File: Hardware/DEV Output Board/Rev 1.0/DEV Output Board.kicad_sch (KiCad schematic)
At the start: 7 parts, among them J1 SPEAKER, J2 SERIAL, U1 Waveshare 2.4in LCD Header, U2 Teensy4.0, U3 Waveshare 2.4in LCD

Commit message: Add BOMs
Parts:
- U1: now in the parts list
- U2: Other (none) -> https://www.pjrc.com/store/teensy40.html
- U3: Other (none) -> https://www.amazon.com/dp/B08H24H7KX; now in the parts list
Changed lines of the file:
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@@
+			)
+		)
+		(property "Digikey" ""
+			(at 209.55 127 0)
+			(hide yes)
+			(show_name no)
+			(do_not_autoplace no)
+			(effects
+				(font
+					(size 1.27 1.27)
+				)
+			)
+		)
+		(property "Other" ""
+			(at 209.55 127 0)
+			(hide yes)
+			(show_name no)
+			(do_not_autoplace no)
+			(effects
+				(font
+					(size 1.27 1.27)
+				)
 			)
 		)
@@
 		(body_style 1)
 		(exclude_from_sim no)
-		(in_bom no)
+		(in_bom yes)
 		(on_board yes)
 		(in_pos_files yes)
@@
 		)
 		(property "Description" ""
+			(at 220.98 72.39 0)
+			(hide yes)
+			(show_name no)
+			(do_not_autoplace no)
+			(effects
+				(font
+					(size 1.27 1.27)
+				)
+			)
+		)
+		(property "Digikey" ""
+			(at 220.98 72.39 0)
+			(hide yes)
+			(show_name no)
+			(do_not_autoplace no)
+			(effects
+				(font
+					(size 1.27 1.27)
+				)
+			)
+		)
+		(property "Other" ""
 			(at 220.98 72.39 0)
 			(hide yes)
@@
 		)
 		(property "Description" "Generic connector, single row, 01x04, script generated (kicad-library-utils/schlib/autogen/connector/)"
+			(at 82.55 163.83 0)
+			(hide yes)
+			(show_name no)
+			(do_not_autoplace no)
+			(effects
+				(font
+					(size 1.27 1.27)
+				)
+			)
+		)
+		(property "Digikey" ""
+			(at 82.55 163.83 0)
+			(hide yes)
+			(show_name no)
+			(do_not_autoplace no)
+			(effects
+				(font
+					(size 1.27 1.27)
+				)
+			)
+		)
+		(property "Other" ""
 			(at 82.55 163.83 0)
 			(hide yes)
@@
 			)
 		)
+		(property "Digikey" ""
+			(at 196.85 134.62 90)
+			(hide yes)
+			(show_name no)
+			(do_not_autoplace no)
+			(effects
+				(font
+					(size 1.27 1.27)
+				)
+			)
+		)
+		(property "Other" ""
+			(at 196.85 134.62 90)
+			(hide yes)
+			(show_name no)
+			(do_not_autoplace no)
+			(effects
+				(font
+					(size 1.27 1.27)
+				)
+			)
+		)
 		(pin "1"
 		)
@@
 		(property "Description" "Resistor"
 			(at 190.5 127 0)
+			(hide yes)
+			(show_name no)
+			(do_not_autoplace no)
+			(effects
+				(font
+					(size 1.27 1.27)
+				)
+			)
+		)
+		(property "Digikey" ""
+			(at 190.5 127 90)
+			(hide yes)
+			(show_name no)
+			(do_not_autoplace no)
+			(effects
+				(font
+					(size 1.27 1.27)
+				)
+			)
+		)
+		(property "Other" ""
+			(at 190.5 127 90)
 			(hide yes)
 			(show_name no)
@@
 			)
 		)
+		(property "Digikey" ""
+			(at 81.28 72.39 0)
+			(hide yes)
+			(show_name no)
+			(do_not_autoplace no)
+			(effects
+				(font
+					(size 1.27 1.27)
+				)
+			)
+		)
+		(property "Other" "https://www.pjrc.com/store/teensy40.html"
+			(at 81.28 72.39 0)
+			(hide yes)
+			(show_name no)
+			(do_not_autoplace no)
+			(effects
+				(font
+					(size 1.27 1.27)
+				)
+			)
+		)
 		(pin "19"
 		)
@@
 		(body_style 1)
 		(exclude_from_sim no)
-		(in_bom no)
+		(in_bom yes)
 		(on_board yes)
 		(in_pos_files yes)
@@
 			(at 170.18 71.12 0)
 			(hide yes)
+			(show_name no)
+			(do_not_autoplace no)
+			(effects
+				(font
+					(size 1.27 1.27)
+				)
+			)
+		)
+		(property "Digikey" ""
+			(at 170.18 71.12 0)
+			(hide yes)
+			(show_name no)
+			(do_not_autoplace no)
+			(effects
+				(font
+					(size 1.27 1.27)
+				)
+			)
+		)
+		(property "Other" "https://www.amazon.com/dp/B08H24H7KX"
+			(at 170.18 71.12 0)
+			(hide yes)

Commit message: Finish BOM and add to README
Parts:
- C1: Other (none) -> https://www.amazon.com/PANMILED-Multilayer-Monolithic-Capac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
- J1: Digikey (none) -> 455-2247-ND
- J2, U1: Other (none) -> https://www.amazon.com/Straight-Breakaway-Connector-Breadbo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
- R6: Digikey (none) -> RNF18FTD1K00CT-ND; Other (none) -> https://www.amazon.com/ALLECIN-8W-Metal-Film-Resistor/dp/B0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
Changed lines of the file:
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@@
 			)
 		)
-		(property "Digikey" ""
+		(property "Digikey" "455-2247-ND"
 			(at 209.55 127 0)
 			(hide yes)
@@
 		)
 		(property "Other" ""
+			(at 209.55 127 0)
+			(hide yes)
+			(show_name no)
+			(do_not_autoplace no)
+			(effects
+				(font
+					(size 1.27 1.27)
+				)
+			)
+		)
+		(property "Mouser" ""
 			(at 209.55 127 0)
 			(hide yes)
@@
 			)
 		)
-		(property "Other" ""
+		(property "Other" "https://www.amazon.com/Straight-Breakaway-Connector-Breadboard-Electronic/dp/B0FRZW75VS"
+			(at 220.98 72.39 0)
+			(hide yes)
+			(show_name no)
+			(do_not_autoplace no)
+			(effects
+				(font
+					(size 1.27 1.27)
+				)
+			)
+		)
+		(property "Mouser" ""
 			(at 220.98 72.39 0)
 			(hide yes)
@@
 			)
 		)
-		(property "Other" ""
+		(property "Other" "https://www.amazon.com/Straight-Breakaway-Connector-Breadboard-Electronic/dp/B0FRZW75VS"
+			(at 82.55 163.83 0)
+			(hide yes)
+			(show_name no)
+			(do_not_autoplace no)
+			(effects
+				(font
+					(size 1.27 1.27)
+				)
+			)
+		)
+		(property "Mouser" ""
 			(at 82.55 163.83 0)
 			(hide yes)
@@
 			)
 		)
-		(property "Other" ""
+		(property "Other" "https://www.amazon.com/PANMILED-Multilayer-Monolithic-Capacitors-Assortment/dp/B0CYQ1Z4G5"
+			(at 196.85 134.62 90)
+			(hide yes)
+			(show_name no)
+			(do_not_autoplace no)
+			(effects
+				(font
+					(size 1.27 1.27)
+				)
+			)
+		)
+		(property "Mouser" ""
 			(at 196.85 134.62 90)
 			(hide yes)
@@
 			)
 		)
-		(property "Digikey" ""
+		(property "Digikey" "RNF18FTD1K00CT-ND"
 			(at 190.5 127 90)
 			(hide yes)
@@
 			)
 		)
-		(property "Other" ""
+		(property "Other" "https://www.amazon.com/ALLECIN-8W-Metal-Film-Resistor/dp/B0C77TM3NR"
+			(at 190.5 127 90)
+			(hide yes)
+			(show_name no)
+			(do_not_autoplace no)
+			(effects
+				(font
+					(size 1.27 1.27)
+				)
+			)
+		)
+		(property "Mouser" ""
 			(at 190.5 127 90)
 			(hide yes)
@@
 			)
 		)
+		(property "Mouser" ""
+			(at 81.28 72.39 0)
+			(hide yes)
+			(show_name no)
+			(do_not_autoplace no)
+			(effects
+				(font
+					(size 1.27 1.27)
+				)
+			)
+		)
 		(pin "19"
 		)
@@
 			(at 170.18 71.12 0)
 			(hide yes)
+			(show_name no)
+			(do_not_autoplace no)
+			(effects
+				(font
+					(size 1.27 1.27)
+				)
+			)
+		)
+		(property "Mouser" ""
+			(at 170.18 71.12 0)
+			(hide yes)

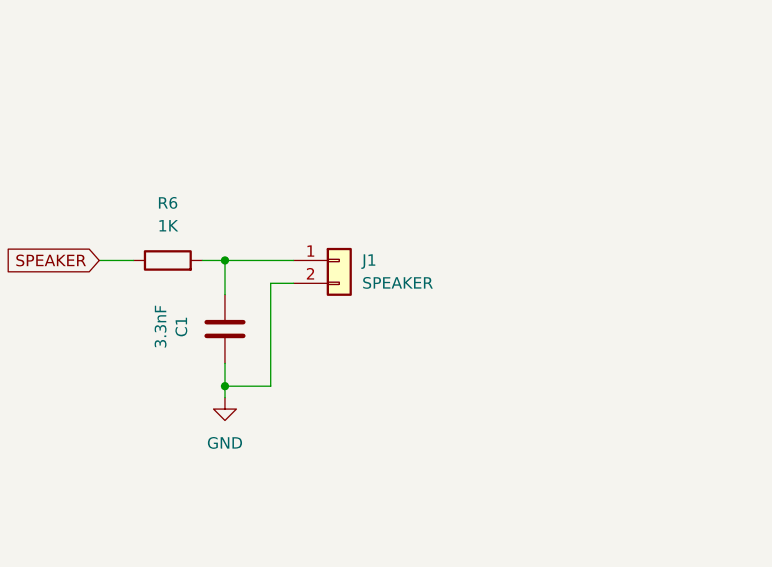
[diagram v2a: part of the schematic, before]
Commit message: Update Dev Output Board silkscreen
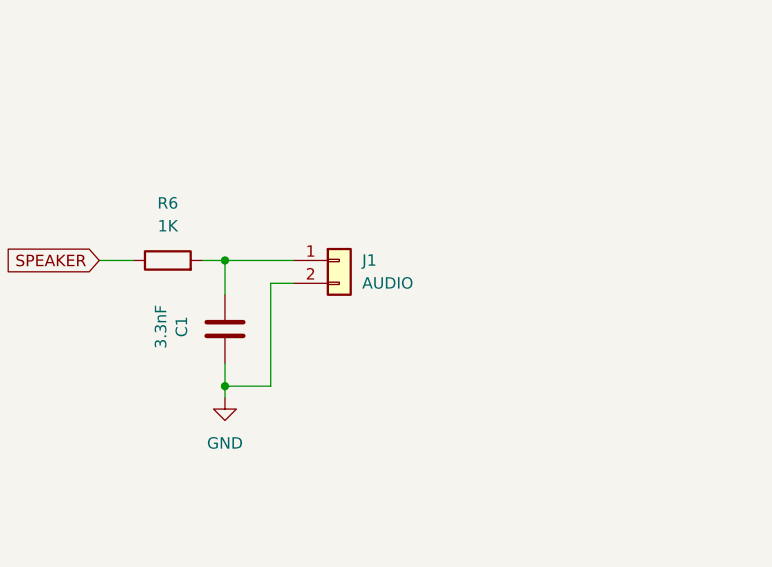
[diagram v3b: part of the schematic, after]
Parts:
- J1: value SPEAKER -> AUDIO
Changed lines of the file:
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@@
 			)
 		)
-		(property "Value" "SPEAKER"
+		(property "Value" "AUDIO"
 			(at 212.09 129.5399 0)
 			(show_name no)
